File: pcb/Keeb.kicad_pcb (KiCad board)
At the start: 2 copper layers, 164 x 102.9 mm, 99 parts, among them J1 TRRS_SJ1-42514, J2 TRRS_SJ1-42514, K00 KEYSW, K01 KEYSW, K02 KEYSW, K03 KEYSW, K04 KEYSW, K05 KEYSW, K10 KEYSW, K11 KEYSW, K12 KEYSW, K13 KEYSW, K14 KEYSW, K15 KEYSW, K20 KEYSW, K21 KEYSW, K22 KEYSW, K23 KEYSW, K24 KEYSW, K25 KEYSW, K26 KEYSW, K27 KEYSW, K30 KEYSW, K31 KEYSW, K32 KEYSW, K33 KEYSW, K34 KEYSW, K35 KEYSW, K36 KEYSW, K37 KEYSW, SW1 SW_RST, U1 ATMEGA32U4, U2 PI6ULS5V9511AWEX_I2C_HotSwap, U3 MCP23017_SO, X1 XTAL_GND

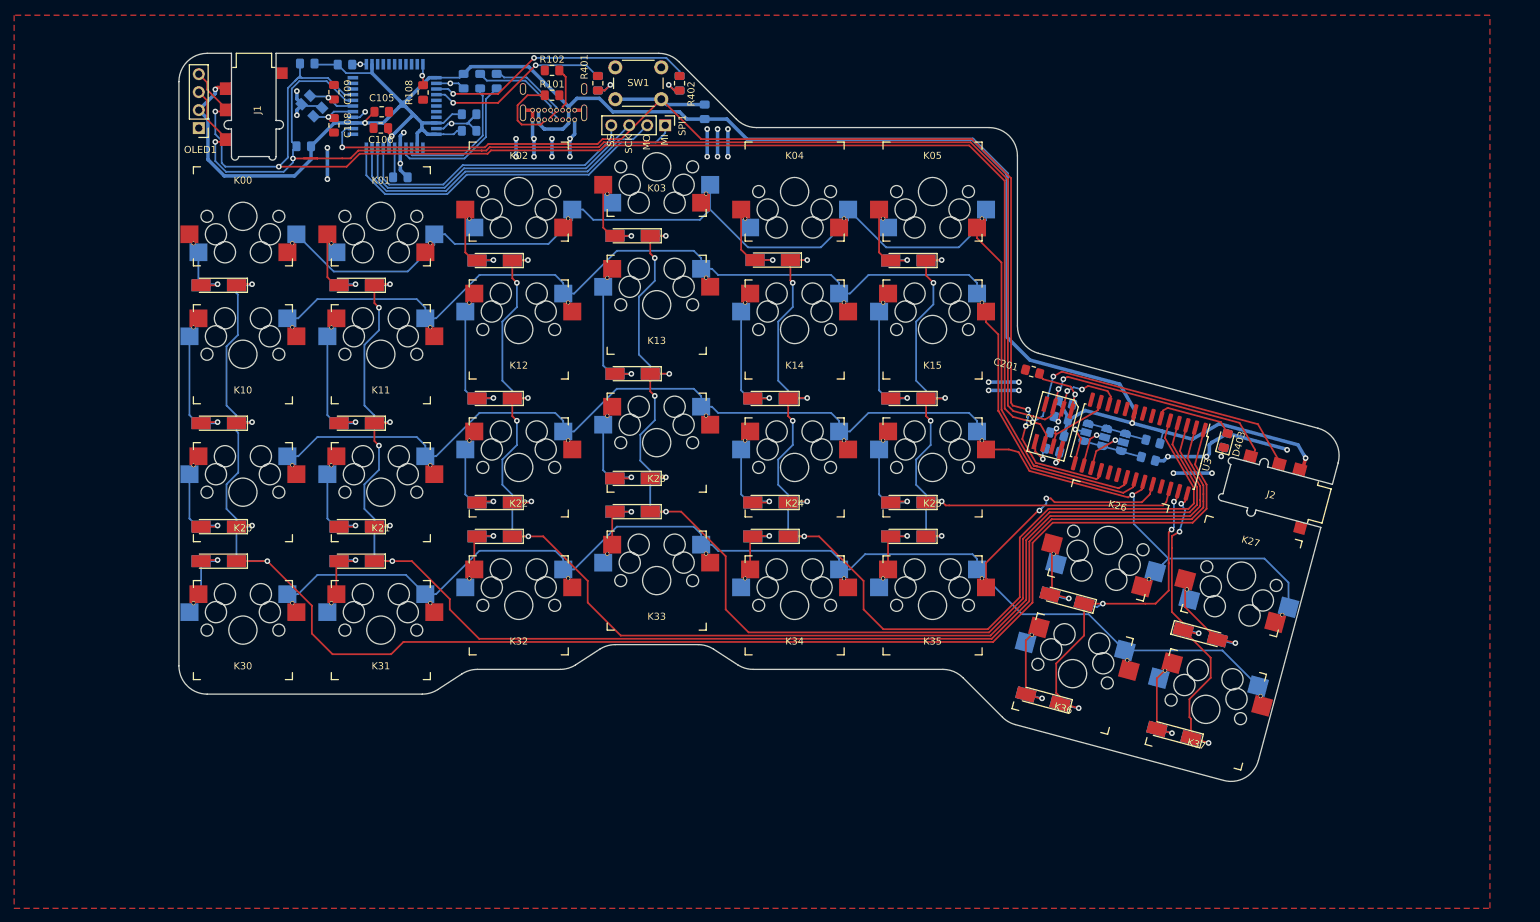
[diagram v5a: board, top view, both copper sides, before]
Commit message: Fixed layout to support trackball over SPI
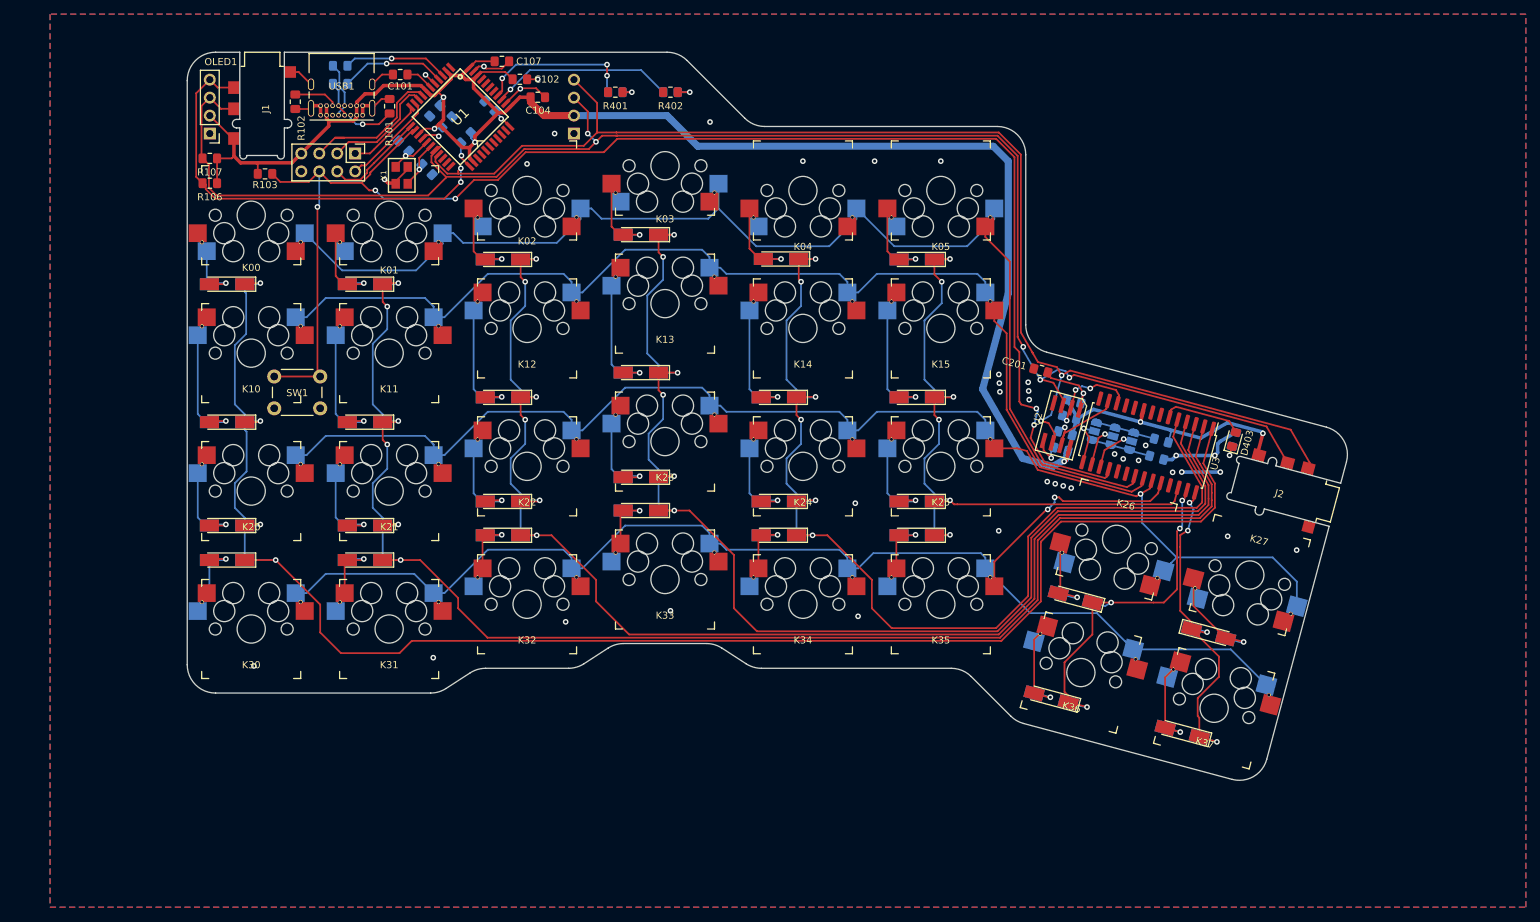
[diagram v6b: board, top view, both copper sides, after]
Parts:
- removed the OLED1 at (199.5, 42.4)
- added OLED1: Conn_01x04, Connector_PinHeader_2.54mm:PinHeader_1x04_P2.54mm_Vertical, F.Cu at (201.1, 43.2)
- added OLED1: Conn_01x04, Connector_PinHeader_2.54mm:PinHeader_1x04_P2.54mm_Vertical, B.Cu at (252.5, 43.2)
- C101, C102, C104, C107, R103, R106, R107, U1, USB1, X1: moved to F.Cu
- C105, C106, C108, C109, R108: moved to B.Cu
- SPI1: footprint Connector_PinHeader_2.54mm:PinHeader_1x04_P2.54mm_Vertical -> Connector_PinHeader_2.54mm:PinHeader_2x04_P2.54mm_Vertical
- moved SW1 63.8 mm to (216.7, 82.1), turned to 180 degrees
- moved R103 62.8 mm to (208.9, 48.9), turned to 0 degrees
- moved SPI1 44.0 mm to (221.6, 46.0)
- moved R102 36.6 mm to (213.1, 38.7), turned to 90 degrees
- moved USB1 24.0 mm to (222.7, 40.6), turned to 180 degrees
- moved R101 23.0 mm to (226.5, 39.3), turned to 270 degrees
- moved R105 22.1 mm to (219.5, 36.2), turned to 180 degrees
- moved R106 21.8 mm to (201.1, 50.2)
- moved C103 20.0 mm to (237.3, 43.8), turned to 225 degrees
- moved R104 19.9 mm to (219.5, 33.6), turned to 180 degrees
- moved C109 17.1 mm to (231.8, 48.3), turned to 315 degrees
- moved X1 16.0 mm to (228.2, 49.1), turned to 270 degrees
- moved C101 14.5 mm to (228.0, 34.9), turned to 180 degrees
- moved R107 13.4 mm to (201.1, 46.7)
- moved C107 10.9 mm to (242.4, 33.0)
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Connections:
- J1 pad 2: SCL -> VCC
- J1 pad 3: SDA -> SCL
- J1 pad 4: VCC -> SDA
- J2 pad 2: SCL -> VCC
- J2 pad 3: SDA -> SCL
- J2 pad 4: VCC -> SDA
- SPI1 pad 4: /SS -> /SS2
- U1 pad 12: Net-(U1-Pad12) -> /SS2
- U1 pad 8: /SS -> /SS1
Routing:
- net /RST: track 171.9 -> 215.2 mm, vias 3 -> 5
- net /SS: track 41.5 -> 0.00 mm
- net /MISO: track 51.9 -> 11.4 mm
- net GND: track 103.6 -> 63.2 mm, vias 33 -> 41
- net /MOSI: track 47.7 -> 13.9 mm
- net /SCK: track 44.0 -> 17.5 mm
- net /SS1: track 0.00 -> 21.3 mm
- net VCC: track 302.0 -> 286.1 mm
- net /SS2: track 0.00 -> 14.6 mm
- net /NumLock: track 38.2 -> 25.9 mm, vias 2 -> 1
- net /UsbD+: track 12.5 -> 5.13 mm
- net Net-(R105-Pad1): track 21.3 -> 15.0 mm, vias 0 -> 1
- net /UsbD-: track 14.1 -> 8.02 mm
- net Net-(R104-Pad1): track 19.1 -> 14.9 mm, vias 0 -> 1
- net Net-(R101-Pad2): track 11.0 -> 6.95 mm, vias 0 -> 1
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- added copper zone on B.Cu, net GND
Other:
- outline, holes or cut-outs redrawn
- board text added: "RST"
- board text added: "SS1"
- board text added: "SS2"
- board text removed: "SCL"
- board text removed: "SDA"
- board text removed: "SS"

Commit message: Fixed issues from test branch
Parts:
- removed D27, D37: D, SVastaCustomParts:D_MiniMELF_Handsoldering_Shorter_Pads_DoubleSided
- removed K27, K37: KEYSW, SVastaCustomParts:Kailh_socket_reversible
- C201: moved to B.Cu
- moved J2 52.5 mm to (322.9, 50.2), turned to 270 degrees
- moved D403 35.3 mm to (322.9, 59.6), turned to 0 degrees
- moved R403 35.3 mm to (322.9, 59.6), turned to 0 degrees
- moved R204 19.7 mm to (318.1, 68.4), turned to 270 degrees
- moved R203 18.5 mm to (315.1, 68.4), turned to 90 degrees
- moved R302 17.0 mm to (319.0, 83.0), turned to 270 degrees
- moved U2 16.1 mm to (321.0, 68.4), turned to 90 degrees
- moved R202 15.5 mm to (326.8, 68.4), turned to 90 degrees
- moved U3 14.1 mm to (321.0, 81.1), turned to 180 degrees
- moved R301 13.1 mm to (322.9, 83.0), turned to 270 degrees
- moved JP0 13.1 mm to (321.0, 73.3), turned to 180 degrees
- moved JP2 12.9 mm to (321.0, 79.1), turned to 180 degrees
- moved R201 12.7 mm to (323.9, 68.4), turned to 90 degrees
- moved JP1 12.5 mm to (321.0, 76.2), turned to 180 degrees
- moved D04 11.7 mm to (293.5, 60.9)
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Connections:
- D00 pad 1: /SwitchMatrix/Col0 -> /SwitchMatrix/Row0
- D01 pad 1: /SwitchMatrix/Col1 -> /SwitchMatrix/Row0
- D02 pad 1: /SwitchMatrix/Col2 -> /SwitchMatrix/Row0
- D03 pad 1: /SwitchMatrix/Col3 -> /SwitchMatrix/Row0
- D04 pad 1: /SwitchMatrix/Col4 -> /SwitchMatrix/Row0
- D05 pad 1: /SwitchMatrix/Col5 -> /SwitchMatrix/Row0
- D10 pad 1: /SwitchMatrix/Col0 -> /SwitchMatrix/Row1
- D11 pad 1: /SwitchMatrix/Col1 -> /SwitchMatrix/Row1
- D12 pad 1: /SwitchMatrix/Col2 -> /SwitchMatrix/Row1
- D13 pad 1: /SwitchMatrix/Col3 -> /SwitchMatrix/Row1
- D14 pad 1: /SwitchMatrix/Col4 -> /SwitchMatrix/Row1
- D15 pad 1: /SwitchMatrix/Col5 -> /SwitchMatrix/Row1
- D20 pad 1: /SwitchMatrix/Col0 -> /SwitchMatrix/Row2
- D21 pad 1: /SwitchMatrix/Col1 -> /SwitchMatrix/Row2
- D22 pad 1: /SwitchMatrix/Col2 -> /SwitchMatrix/Row2
- D23 pad 1: /SwitchMatrix/Col3 -> /SwitchMatrix/Row2
- D24 pad 1: /SwitchMatrix/Col4 -> /SwitchMatrix/Row2
- D25 pad 1: /SwitchMatrix/Col5 -> /SwitchMatrix/Row2
- D26 pad 1: /SwitchMatrix/Col6 -> /SwitchMatrix/Row2
- D30 pad 1: /SwitchMatrix/Col0 -> /SwitchMatrix/Row3
- D31 pad 1: /SwitchMatrix/Col1 -> /SwitchMatrix/Row3
- D32 pad 1: /SwitchMatrix/Col2 -> /SwitchMatrix/Row3
- D33 pad 1: /SwitchMatrix/Col3 -> /SwitchMatrix/Row3
- D34 pad 1: /SwitchMatrix/Col4 -> /SwitchMatrix/Row3
- D35 pad 1: /SwitchMatrix/Col5 -> /SwitchMatrix/Row3
- D36 pad 1: /SwitchMatrix/Col6 -> /SwitchMatrix/Row3
- K00 pad 1: Net-(D00-Pad2) -> /SwitchMatrix/Col0
- K00 pad 2: /SwitchMatrix/Row0 -> Net-(D00-Pad2)
- K01 pad 1: Net-(D01-Pad2) -> /SwitchMatrix/Col1
- K01 pad 2: /SwitchMatrix/Row0 -> Net-(D01-Pad2)
- K02 pad 1: Net-(D02-Pad2) -> /SwitchMatrix/Col2
- K02 pad 2: /SwitchMatrix/Row0 -> Net-(D02-Pad2)
- K03 pad 1: Net-(D03-Pad2) -> /SwitchMatrix/Col3
- K03 pad 2: /SwitchMatrix/Row0 -> Net-(D03-Pad2)
- K04 pad 1: Net-(D04-Pad2) -> /SwitchMatrix/Col4
- K04 pad 2: /SwitchMatrix/Row0 -> Net-(D04-Pad2)
- K05 pad 1: Net-(D05-Pad2) -> /SwitchMatrix/Col5
- K05 pad 2: /SwitchMatrix/Row0 -> Net-(D05-Pad2)
- K10 pad 1: /SwitchMatrix/Row1 -> /SwitchMatrix/Col0
- K11 pad 1: /SwitchMatrix/Row1 -> /SwitchMatrix/Col1
- K12 pad 1: /SwitchMatrix/Row1 -> /SwitchMatrix/Col2
- K13 pad 1: /SwitchMatrix/Row1 -> /SwitchMatrix/Col3
- K14 pad 1: /SwitchMatrix/Row1 -> /SwitchMatrix/Col4
- K15 pad 1: /SwitchMatrix/Row1 -> /SwitchMatrix/Col5
- K20 pad 1: /SwitchMatrix/Row2 -> /SwitchMatrix/Col0
- K21 pad 1: /SwitchMatrix/Row2 -> /SwitchMatrix/Col1
- K22 pad 1: /SwitchMatrix/Row2 -> /SwitchMatrix/Col2
- K23 pad 1: /SwitchMatrix/Row2 -> /SwitchMatrix/Col3
- K24 pad 1: /SwitchMatrix/Row2 -> /SwitchMatrix/Col4
- K25 pad 1: /SwitchMatrix/Row2 -> /SwitchMatrix/Col5
- K26 pad 1: Net-(D26-Pad2) -> /SwitchMatrix/Col6
- K26 pad 2: /SwitchMatrix/Row2 -> Net-(D26-Pad2)
- K30 pad 1: /SwitchMatrix/Row3 -> /SwitchMatrix/Col0
- K31 pad 1: /SwitchMatrix/Row3 -> /SwitchMatrix/Col1
- K32 pad 1: /SwitchMatrix/Row3 -> /SwitchMatrix/Col2
- K33 pad 1: /SwitchMatrix/Row3 -> /SwitchMatrix/Col3
- K34 pad 1: /SwitchMatrix/Row3 -> /SwitchMatrix/Col4
- K35 pad 1: /SwitchMatrix/Row3 -> /SwitchMatrix/Col5
- K36 pad 1: /SwitchMatrix/Row3 -> /SwitchMatrix/Col6
- U3 pad 26: /SwitchMatrix/Col5 -> Net-(U3-Pad26)
- U3 pad 27: /SwitchMatrix/Col6 -> Net-(U3-Pad27)
- U3 pad 28: /SwitchMatrix/Col7 -> /IO_Connected
- U3 pad 6: /IO_Connected -> /SwitchMatrix/Col5
- U3 pad 7: Net-(U3-Pad7) -> /SwitchMatrix/Col6
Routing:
- net SDA: track 245.2 -> 185.6 mm, vias 4 -> 2
- net SCL: track 229.8 -> 179.1 mm, vias 5 -> 4
- net /SwitchMatrix/Row0: track 191.2 -> 140.8 mm, vias 0 -> 6
- net /SwitchMatrix/Col7: track 49.2 -> 0.00 mm, vias 4 -> 0
- net /SwitchMatrix/Row1: track 173.6 -> 131.8 mm, vias 0 -> 6
- net /SwitchMatrix/Row3: track 216.0 -> 174.6 mm, vias 2 -> 7
- net VCC: track 286.1 -> 248.1 mm
- net /SwitchMatrix/Row2: track 200.5 -> 162.5 mm, vias 1 -> 7
- net /IO_Connected: track 11.6 -> 41.6 mm, vias 0 -> 2
- net /SwitchMatrix/Col0: track 229.8 -> 201.6 mm, vias 4 -> 0
- net /SwitchMatrix/Col3: track 173.0 -> 145.3 mm, vias 6 -> 0
- net /RST: track 215.2 -> 187.8 mm, vias 5 -> 3
- net /SwitchMatrix/Col2: track 188.8 -> 162.9 mm, vias 6 -> 0
- net /SwitchMatrix/Col4: track 150.7 -> 124.9 mm, vias 6 -> 0
- net /SwitchMatrix/Col1: track 205.8 -> 180.4 mm, vias 6 -> 0
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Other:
- board size 164 x 102.9 mm -> 142.6 x 98.1 mm

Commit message: restarted layout
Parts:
- removed J1: TRRS_SJ1-42514, SVastaCustomParts:3.5mm_Cut_out
- removed JP0, JP1, JP2: SolderJumper_3_Open, Jumper:SolderJumper-3_P1.3mm_Open_RoundedPad1.0x1.5mm
- removed the OLED1 at (201.1, 43.2)
- removed the OLED1 at (252.5, 43.2)
- added 1: SolderJumper_3_Open, Jumper:SolderJumper-3_P1.3mm_Open_RoundedPad1.0x1.5mm, B.Cu at (320.0, 70.4)
- added 2: SolderJumper_3_Open, Jumper:SolderJumper-3_P1.3mm_Open_RoundedPad1.0x1.5mm, B.Cu at (320.0, 73.3)
- added 4: SolderJumper_3_Open, Jumper:SolderJumper-3_P1.3mm_Open_RoundedPad1.0x1.5mm, B.Cu at (320.0, 76.2)
- added D401: CAPS, LED_SMD:LED_0805_2012Metric_Pad1.15x1.40mm_HandSolder, F.Cu at (325.9, 102.0)
- added D402: NUM, LED_SMD:LED_0805_2012Metric_Pad1.15x1.40mm_HandSolder, F.Cu at (322.0, 102.0)
- added D403: CONN, LED_SMD:LED_0805_2012Metric_Pad1.15x1.40mm_HandSolder, B.Cu at (318.1, 102.0)
- added G***: LOGO, SVastaCustomParts:wing_it_400dpi, B.Cu at (215.2, 48.9)
- added OLED1: Conn_01x04, Connector_PinHeader_2.54mm:PinHeader_1x04_P2.54mm_Vertical, B.Cu at (323.9, 59.6)
- added OLED1: Conn_01x04, Connector_PinHeader_2.54mm:PinHeader_1x04_P2.54mm_Vertical, F.Cu at (323.9, 93.8)
- C101, R106: moved to B.Cu
- K26, K36: footprint SVastaCustomParts:Kailh_socket_reversible -> SVastaCustomParts:switch_off_board
- moved R103 133.2 mm to (341.5, 61.6), turned to 270 degrees
- moved SPI1 123.4 mm to (337.6, 87.9)
- moved SW1 118.2 mm to (333.7, 99.6)
- moved C101 117.0 mm to (338.5, 73.3), turned to 270 degrees
- moved R107 116.4 mm to (317.1, 55.7)
- moved R106 116.2 mm to (317.1, 55.7)
- moved C108 110.7 mm to (337.4, 64.7), turned to 0 degrees
- moved C106 109.7 mm to (338.5, 69.4), turned to 90 degrees
- moved C107 108.6 mm to (338.6, 83.4), turned to 270 degrees
- moved X1 107.2 mm to (334.6, 61.6), turned to 135 degrees
- moved C105 104.8 mm to (335.6, 69.4), turned to 90 degrees
- moved U1 103.4 mm to (334.6, 73.3), turned to 180 degrees
- moved C109 102.2 mm to (332.7, 64.7), turned to 180 degrees
- moved C102 101.7 mm to (334.7, 83.4), turned to 90 degrees
- moved R104 101.4 mm to (320.0, 47.6)
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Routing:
- net /RST: track 187.8 -> 76.9 mm, vias 3 -> 4
- net SCL: track 179.1 -> 79.2 mm, vias 4 -> 3
- net SDA: track 185.6 -> 105.9 mm, vias 2 -> 5
- net VCC: track 248.1 -> 175.4 mm
- net GND: track 45.4 -> 79.9 mm, vias 55 -> 42
- net Net-(R104-Pad1): track 14.9 -> 43.4 mm
- net Net-(R105-Pad1): track 15.0 -> 43.4 mm
- net /SwitchMatrix/Row3: track 174.6 -> 147.1 mm, vias 7 -> 6
- net /SwitchMatrix/Row2: track 162.5 -> 142.4 mm, vias 7 -> 6
- net /IO_Connected: track 41.6 -> 22.3 mm
- net /SwitchMatrix/Col6: track 45.7 -> 28.5 mm
- net Net-(D36-Pad2): track 21.2 -> 5.72 mm, vias 1 -> 0
- net /SS2: track 14.6 -> 28.5 mm, vias 0 -> 1
- net /MISO: track 11.4 -> 23.1 mm, vias 0 -> 1
- net Net-(D26-Pad2): track 16.7 -> 5.84 mm, vias 1 -> 0
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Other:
- board size 142.6 x 98.1 mm -> 145.5 x 73.3 mm
- board text added: "0"
- board text added: "Wing it! Keyboard Designed by Sam Vasta 2020 rev. J"
- board text added: "module address"
